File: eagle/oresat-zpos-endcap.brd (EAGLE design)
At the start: 106 x 106 mm, 47 parts, among them J7 1.27MM-SWD-CONNECTOR, U1 TPS63070, U2 TCAN330, U6 STM32F042K6, X1 16MHZ-2.5x2mm

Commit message: Oh right, the bottom of the board.
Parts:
- flipped CF1 to the bottom
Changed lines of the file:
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@@
 <attribute name="VALUE" x="59.71" y="29.575" size="1.27" layer="27" rot="R180"/>
 </element>
-<element name="CF1" library="oresat-connectors" package="CON-1.27-F-HARTING-1522012X601XXX" value="ORESAT-SOLARPANEL-12PIN" x="11.5" y="84.5" smashed="yes" rot="R90">
-<attribute name="NAME" x="8.325" y="92.485" size="0.635" layer="25" ratio="20" rot="R90"/>
-<attribute name="VALUE" x="9.595" y="92.485" size="0.635" layer="27" ratio="20" rot="R90"/>
+<element name="CF1" library="oresat-connectors" package="CON-1.27-F-HARTING-1522012X601XXX" value="ORESAT-SOLARPANEL-12PIN" x="11.5" y="84.5" smashed="yes" rot="MR90">
+<attribute name="NAME" x="14.675" y="92.485" size="0.635" layer="26" ratio="20" rot="MR90"/>
+<attribute name="VALUE" x="13.405" y="92.485" size="0.635" layer="28" ratio="20" rot="MR90"/>
 </element>
 </elements>

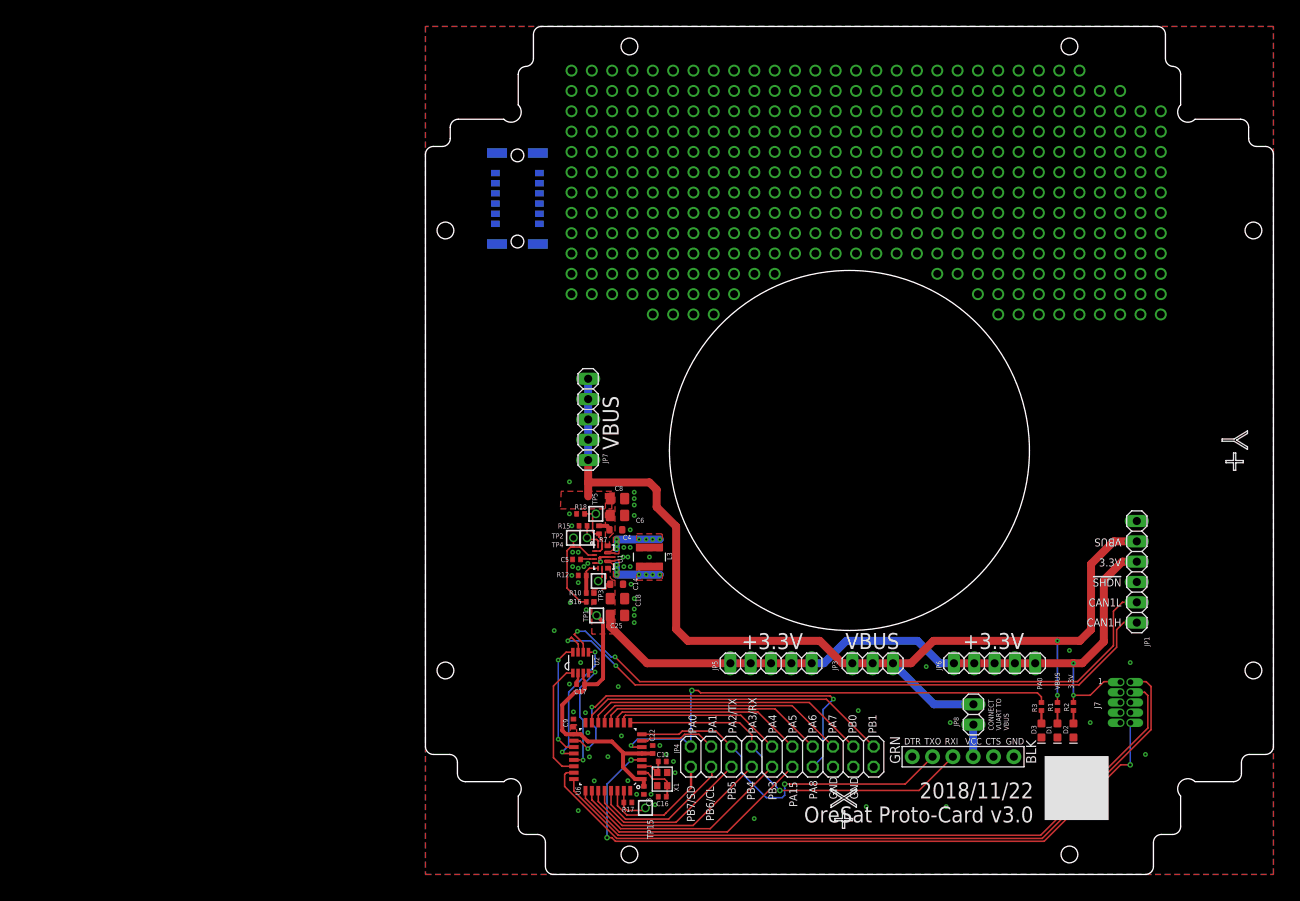
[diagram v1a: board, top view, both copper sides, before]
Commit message: Updated version info on the board and readme, and added picture.
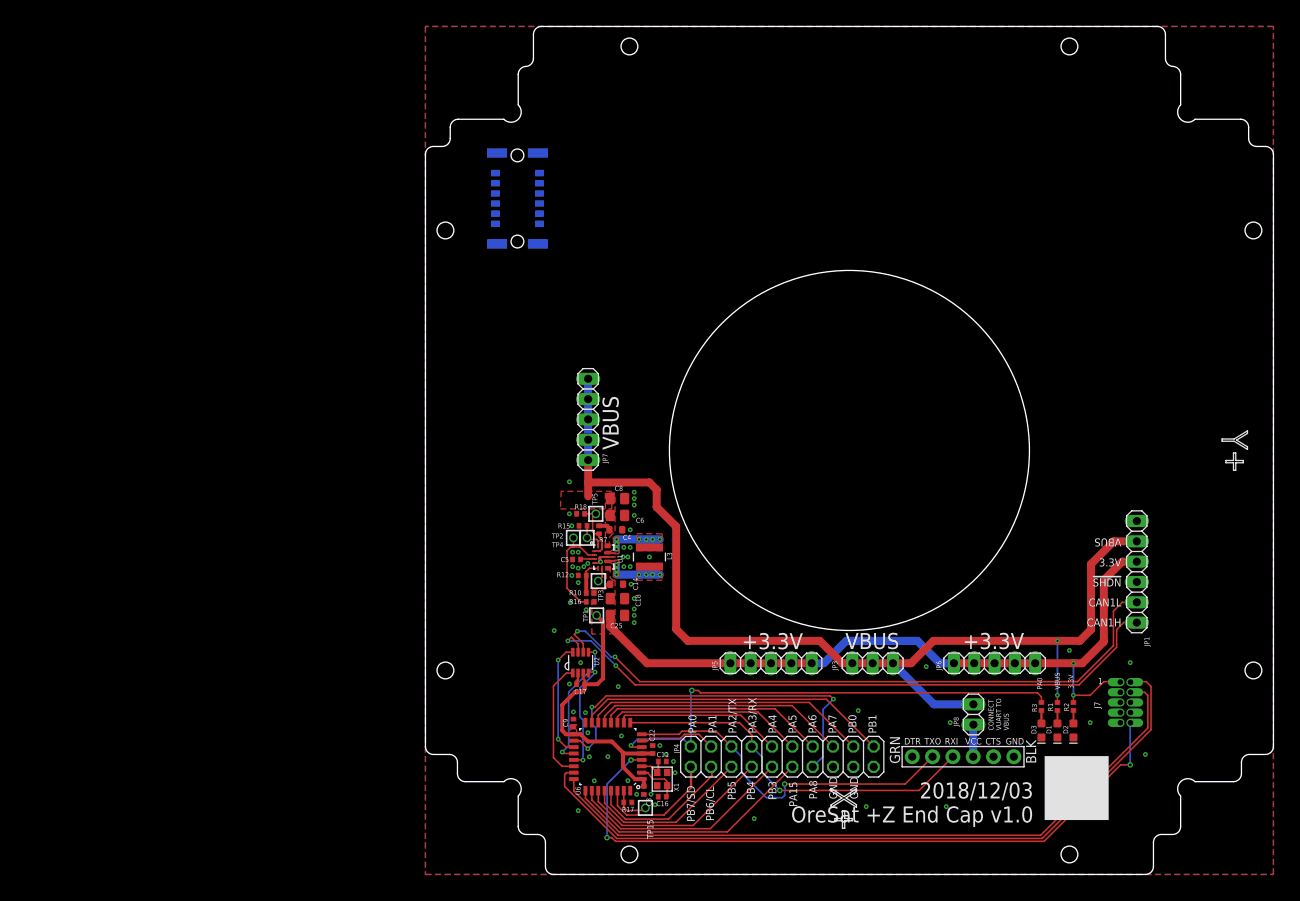
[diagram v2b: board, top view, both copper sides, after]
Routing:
- net GND: vias 114 -> 61
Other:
- board text added: "2018/12/03"
- board text added: "OreSat +Z End Cap v1.0"
- board text removed: "2018/11/22"
- board text removed: "OreSat Proto-Card v3.0"

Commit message: Not done, but checking in anyway. Lots left to do, trying to figure out where things go.
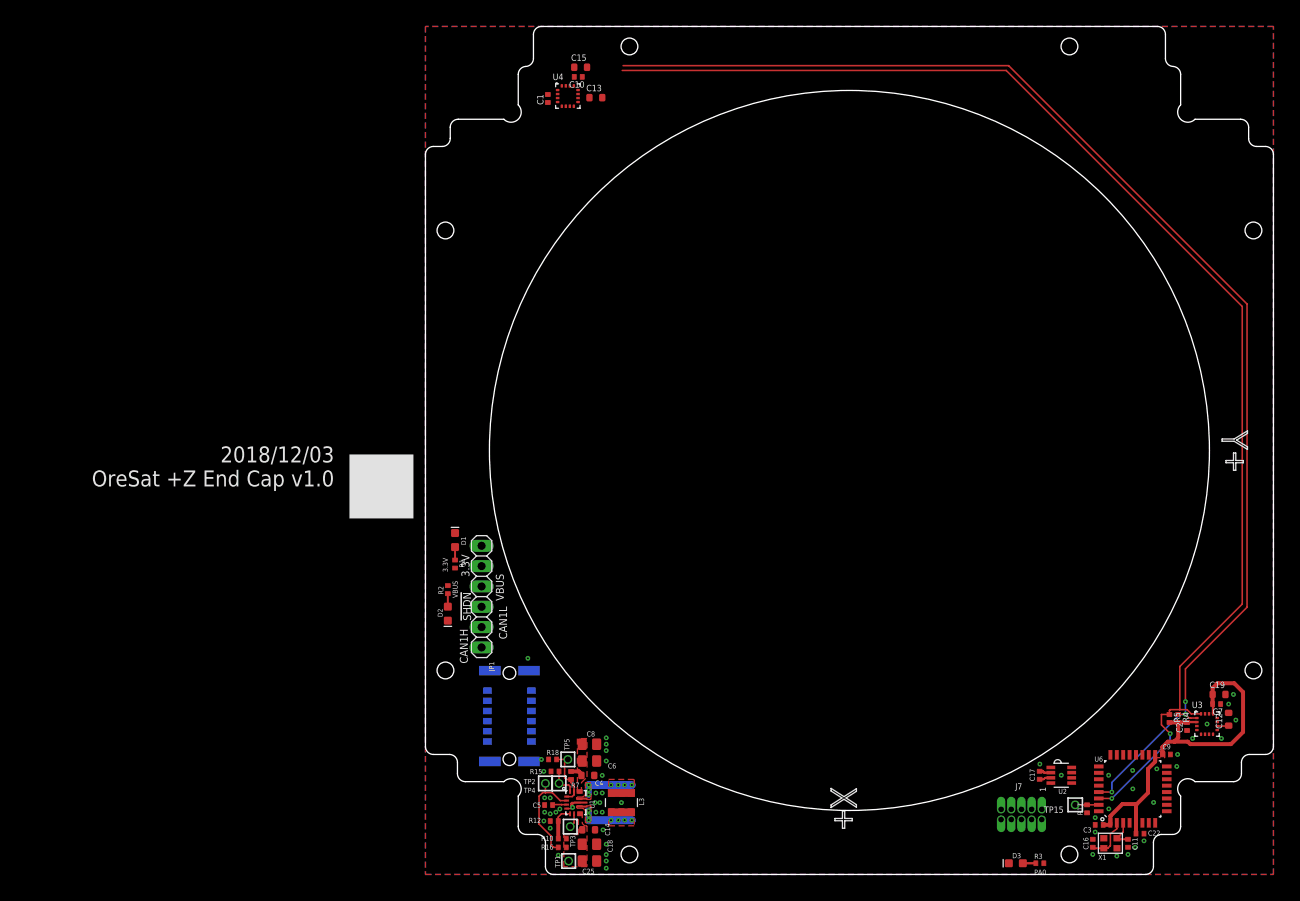
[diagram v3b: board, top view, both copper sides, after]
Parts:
- removed J5: (no value), SparkFun-Connectors:6_PIN_SERIAL_TARGET_SIDE_W_SILK
- removed JP3: (no value), pinhead:1X03
- removed JP4: (no value), pinhead:2X10
- removed JP5, JP6, JP7: (no value), pinhead:1X05
- removed JP8: (no value), pinhead:1X02
- added C1, C10, C2, C7: 100n, rcl_custom:.0402-B-NOSILK
- added C12, C13: 10u, oresat-rcl:.0603-B-NOSILK
- added C15, C19: 4.7u, oresat-rcl:.0603-B-NOSILK
- added R4, R5: 4.7k, rcl_custom:.0402-B-NOSILK
- added U3, U4: HMC5883L, monitor-v2:QLGA-16(3X3)
- CF1: value ORESAT-SOLARPANEL-12PIN -> J-HARWIN-M55-6021242R; device oresat-connectors:CON-1.27-F-HARTING-1522012X601XXX -> J-Harwin-M55-6021242R:HARWIN-M55-6021242R
- moved JP1 82.0 mm to (7.02, 34.7)
- moved D2 79.6 mm to (2.80, 32.6)
- moved R2 79.6 mm to (2.80, 35.6)
- moved D1 79.0 mm to (3.70, 41.8), turned to 90 degrees
- moved R1 77.4 mm to (3.70, 38.8), turned to 270 degrees
- moved C9 74.2 mm to (92.6, 15.0), turned to 180 degrees
- moved U6 65.7 mm to (88.4, 10.7), turned to 90 degrees
- moved CF1 64.7 mm to (10.5, 19.8)
- moved C22 61.8 mm to (89.3, 5.10), turned to 180 degrees
- moved U2 61.7 mm to (79.5, 12.4), turned to 270 degrees
- moved C11 59.1 mm to (87.8, 3.90), turned to 270 degrees
- moved C17 58.5 mm to (76.8, 12.4), turned to 270 degrees
- moved R17 57.4 mm to (82.7, 8.20), turned to 90 degrees
- moved C3 57.1 mm to (84.2, 6.20), turned to 0 degrees
- moved X1 56.6 mm to (85.6, 3.90), turned to 0 degrees
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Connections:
- removed net N$406: J5.P$4, JP8.2
- new net N$2: C12.1, U3.10
- new net N$3: U4.15
- new net N$4: U3.15
- new net N$5: C13.1, U4.10
- net 3.3V: now also C1.2, C10.2, C15.1, C19.1, C2.2, C7.2, R4.2, R5.2, U3.13, U3.2, U4.13, U4.2; no longer JP5.1, JP5.2, JP5.3, JP5.4, JP5.5, JP6.1, JP6.2, JP6.3, JP6.4, JP6.5
- net GND: now also C1.1, C10.1, C12.2, C13.2, C15.2, C19.2, C2.1, C7.1, CF1.P$1, CF1.P$2, CF1.P$3, CF1.P$4, U3.11, U3.9, U4.11, U4.9; no longer J5.P$6, JP4.15, JP4.17, JP4.19
- net PA0: no longer JP4.2
- net PA1: no longer JP4.4
- net PA15: no longer JP4.11
- net PA2/USART2_TX: no longer J5.P$2, JP4.6
- net PA3/USART2_RX: no longer J5.P$3, JP4.8
- net PA4: no longer JP4.10
- net PA5/SPI1_SCK: no longer JP4.12
- net PA6/SPI1_MISO: no longer JP4.14
- net PA7/SPI1_MOSI: no longer JP4.16
- net PA8: no longer JP4.13
- net PB0: no longer JP4.18
- net PB1: no longer JP4.20
- net PB3: no longer JP4.9
- net PB4: no longer JP4.7
- net PB5: no longer JP4.5
- net PB6/SCL: now also R4.1, U3.1, U4.1; no longer JP4.3
- net PB7/SDA: now also R5.1, U3.16, U4.16; no longer JP4.1
- net VBUS: no longer JP3.1, JP3.2, JP3.3, JP7.1, JP7.2, JP7.3, JP7.4, JP7.5, JP8.1
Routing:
- net PB7/SDA: track 15.6 -> 164.8 mm, vias 0 -> 2
- net PB6/SCL: track 18.5 -> 163.0 mm, vias 0 -> 3
- net VBUS: track 134.1 -> 1.62 mm, vias 2 -> 0
- net SWDIO: track 92.6 -> 0.00 mm
- net SWCLK: track 87.5 -> 0.00 mm
- net NRESET: track 87.1 -> 0.00 mm, vias 3 -> 0
- net CAN1_L: track 82.4 -> 0.00 mm, vias 2 -> 0
- net 3.3V: track 130.8 -> 49.0 mm, vias 2 -> 0
- net CAN1_H: track 80.8 -> 0.04 mm, vias 2 -> 0
- net PA0: track 61.4 -> 0.00 mm, vias 2 -> 0
- net PA8: track 48.5 -> 0.00 mm, vias 3 -> 0
- net PA3/USART2_RX: track 47.6 -> 0.00 mm, vias 1 -> 0
- net PA2/USART2_TX: track 44.1 -> 0.00 mm, vias 1 -> 0
- net PB1: track 39.4 -> 0.00 mm
- net PB0: track 35.8 -> 0.00 mm
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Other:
- outline, holes or cut-outs redrawn
- board text removed: "+3.3V"
- board text removed: "CONNECT VUART TO VBUS"
- board text removed: "GND"
- board text removed: "PA1"
- board text removed: "PA15"
- board text removed: "PA2/TX"
- board text removed: "PA3/RX"
- board text removed: "PA4"
- board text removed: "PA5"
- board text removed: "PA6"
- board text removed: "PA7"
- board text removed: "PA8"
- board text removed: "PB0"
- board text removed: "PB1"
- board text removed: "PB3"
- board text removed: "PB4"
- board text removed: "PB5"
- board text removed: "PB6/CL"
- board text removed: "PB7/SD"

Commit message: Removed SPS + uC blocks; only magnetometers remain on the end cap. Not great for future expandability, but moves uC to the end card where it's more useful.
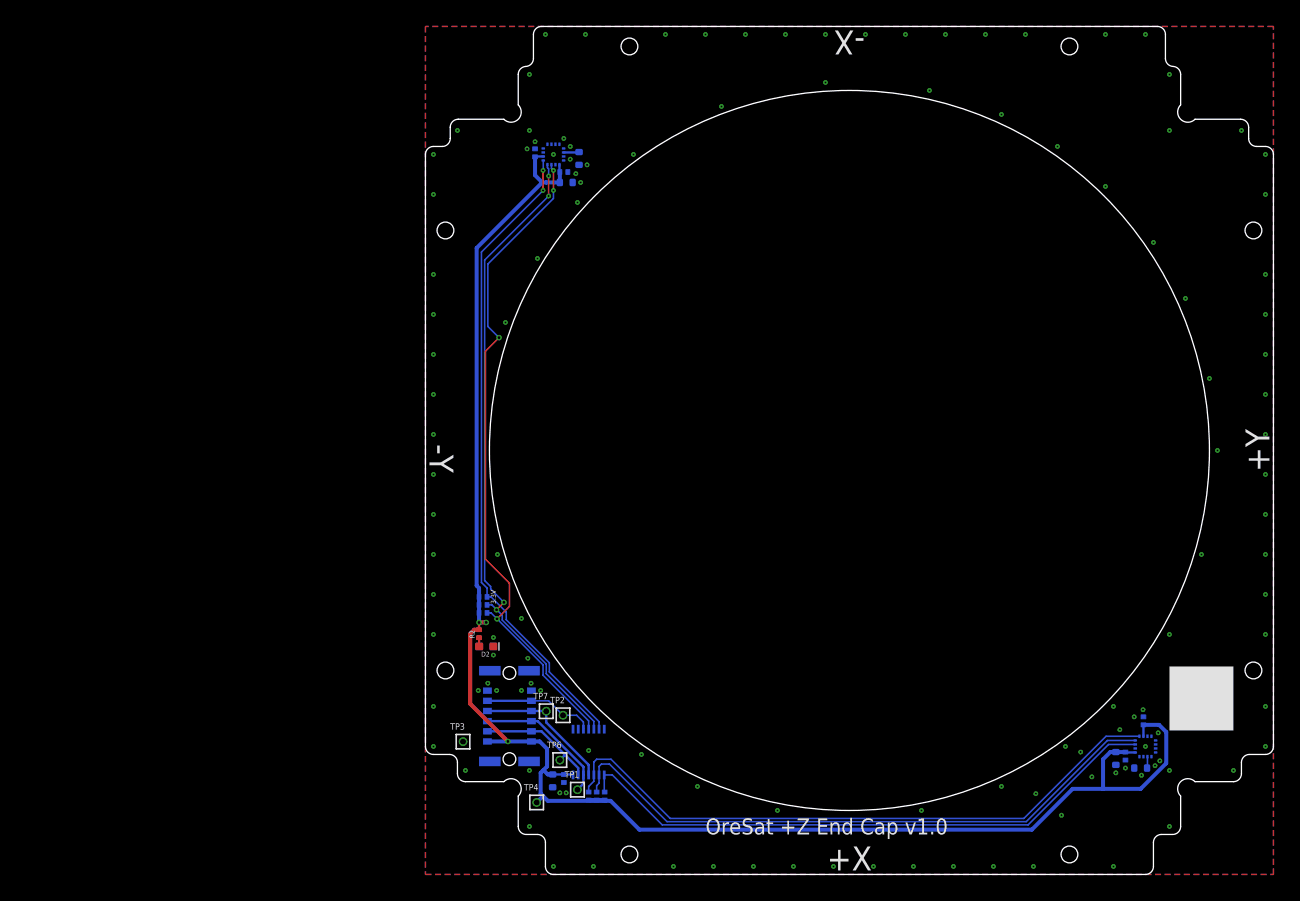
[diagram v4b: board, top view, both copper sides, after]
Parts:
- removed C11, C16: 20p, rcl_custom:.0402-B-NOSILK
- removed C14: 22u, oresat-rcl:.0603-B-NOSILK
- removed C17, C22, C5, C9: 100n, rcl_custom:.0402-B-NOSILK
- removed C18, C25: 22u, oresat-rcl:.0805-B-NOSILK
- removed C6, C8: 10u, oresat-rcl:.0805-B-NOSILK
- removed CF1: J-HARWIN-M55-6021242R, J-Harwin-M55-6021242R:HARWIN-M55-6021242R
- removed D1, D3: GREEN, SparkFun-LED:LED-0603
- removed J7: 1.27MM-SWD-CONNECTOR, J-CNC-3220-10-0100-00-ARM-SWD-port:1.27MM_2X5
- removed JP1: (no value), pinhead:1X06
- removed L3: 1.5 uH, L-Coilcraft-XFL4020:L-COILCRAFT-XFL4020
- removed R10: 470k, rcl_custom:.0402-B-NOSILK
- removed R12: 150k, rcl_custom:.0402-B-NOSILK
- removed R15, R17: 10k, rcl_custom:.0402-B-NOSILK
- removed R16, R18: NP, rcl_custom:.0402-B-NOSILK
- removed TP15, TP5: TEST-POINT, Tova:2MM-TEST-POINT
- removed U2: TCAN330, TCAN330:SOT23-8_TI-DCN
- removed U6: STM32F042K6, STM32F042K:QFP32-7X7
- removed X1: 16MHZ-2.5x2mm, low-gain-radio:CRYSTAL_2.5X2
- added CF2: J-HARWIN-M55-70X1242R, J-Harwin-M55-70X1242R-12pin-1.27mm-M-vertical:HARWIN-M55-70X1242R
- added R6: 4.7k, rcl_custom:.0402-B-NOSILK
- added TP6, TP7: TEST-POINT, Tova:2MM-TEST-POINT
- R1, R3: value 2.7k -> 4.7k
- R7: value 10k -> 4.7k
- U1: value TPS63070 -> TCA9543A-PW; device ic-pwr-tps63070x:TPS63070X -> U-TI-TCA9543A-I2C-2-to-1-multiplexer:TSSOP14-0.65-5.4X4.4MM
- moved R4 88.2 mm to (7.20, 34.7), flipped to the bottom, turned to 0 degrees
- moved R5 87.0 mm to (7.20, 33.7), flipped to the bottom, turned to 0 degrees
- moved C3 67.2 mm to (17.3, 12.0), flipped to the bottom, turned to 270 degrees
- moved R3 55.0 mm to (22.4, 9.80), flipped to the bottom, turned to 270 degrees
- moved TP3 17.1 mm to (4.70, 16.6)
- moved C19 15.2 mm to (86.3, 14.5), flipped to the bottom, turned to 270 degrees
- moved C15 14.5 mm to (17.6, 86.5), flipped to the bottom, turned to 180 degrees
- moved C7 13.1 mm to (87.5, 14.8), flipped to the bottom, turned to 270 degrees
- moved C12 12.6 mm to (89.4, 13.3), flipped to the bottom, turned to 0 degrees
- moved C10 12.0 mm to (17.3, 87.8), flipped to the bottom
- moved TP1 8.99 mm to (19.0, 10.6)
- moved TP2 8.80 mm to (17.2, 19.9)
- moved U3 8.19 mm to (90.0, 16.0), flipped to the bottom, turned to 270 degrees
- moved C13 7.88 mm to (19.2, 89.5), flipped to the bottom, turned to 270 degrees
- moved U4 7.52 mm to (16.0, 90.0), flipped to the bottom, turned to 180 degrees
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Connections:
- removed net BOOT: R17.2, TP15.1, U6.31
- removed net CAN1_H: JP1.1, U2.7
- removed net CAN1_L: JP1.2, U2.6
- removed net CAN_RX: U2.4, U6.21
- removed net CAN_SHDN: U2.5, U6.20
- removed net CAN_SILENT: U2.8, U6.19
- removed net CAN_TX: U2.1, U6.22
- removed net CRYSTALIN: C16.1, U6.2, X1.1
- removed net CRYSTALOUT: C11.1, U6.3, X1.3
- removed net N$1: D3.A, R3.1
- removed net N$270: D1.A, R1.1
- removed net N$3: U4.15
- removed net N$4: U3.15
- removed net NRESET: J7.!RESET, U6.4
- removed net PA0: R3.2, U6.6
- removed net PA1: U6.7
- removed net PA15: U6.25
- removed net PA2/USART2_TX: U6.8
- removed net PA3/USART2_RX: U6.9
- removed net PA4: U6.10
- removed net PA5/SPI1_SCK: U6.11
- removed net PA6/SPI1_MISO: U6.12
- removed net PA7/SPI1_MOSI: U6.13
- removed net PA8: U6.18
- removed net PB0: U6.14
- removed net PB1: U6.15
- removed net PB3: U6.26
- removed net PB4: U6.27
- removed net PB5: U6.28
- removed net PB6/SCL: R4.1, U3.1, U4.1, U6.29
- removed net PB7/SDA: R5.1, U3.16, U4.16, U6.30
- removed net SWCLK: J7.SWDCLK, U6.24
- removed net SWDIO: J7.SWDIO, U6.23
- removed net TPS-EN1: R18.2, R7.1, TP5.1, U1.1, U1.14
- removed net TPS-FB1: R10.1, R12.2, U1.5
- removed net TPS-FB3: TP3.1, U1.6
- removed net TPS-L3: L3.1, U1.11
- removed net TPS-L4: L3.2, U1.9
- removed net TPS-PG1: R16.1, TP2.1, U1.2
- removed net TPS-VAUX1: C5.1, U1.3
- removed net TPS-VSEL1: R15.2, TP4.1, U1.15
- removed net VBUS: C4.1, C6.1, C8.1, JP1.5, R1.2, R7.2, U1.12-13
- new net !I2C-RESET: CF2.3, CF2.4, TP2.1, U1.3
- new net !INT0: R1.1, U1.4, U4.15
- new net !INT1: R3.1, U1.8, U3.15
- new net I2C-!INT: CF2.5, CF2.6, TP7.1, U1.11
- new net I2C-SCL: CF2.7, CF2.8, TP1.1, U1.12
- new net I2C-SDA: CF2.10, CF2.9, TP6.1, U1.13
- new net SC1: R7.1, U1.10, U3.1
- new net SCL0: R4.1, U1.6, U4.1
- new net SD1: R6.1, U1.9, U3.16
- new net SDA0: R5.1, U1.5, U4.16
- net 3.3V: now also C1.1, C10.1, C2.1, C3.1, C4.1, C7.1, CF2.11, CF2.12, R1.2, R3.2, R6.2, R7.2, TP4.1, U1.14; no longer C1.2, C10.2, C14.1, C17.2, C18.1, C2.2, C22.2, C25.1, C3.2, C7.2, C9.2, J7.VTREF, JP1.4, R10.2, R16.2, TP1.1, U1.7-8, U2.3, U6.1, U6.17, U6.5
- net GND: now also C1.2, C10.2, C2.2, C3.2, C7.2, CF2.1, CF2.2, CF2.P$1, CF2.P$2, CF2.P$3, CF2.P$4, TP3.1, U1.1, U1.2, U1.7; no longer C1.1, C10.1, C11.2, C14.2, C16.2, C17.1, C18.2, C2.1, C22.1, C25.2, C3.1, C5.2, C6.2, C7.1, C8.2, C9.1, CF1.P$1, CF1.P$2, CF1.P$3, CF1.P$4, D1.C, D3.C, J7.GND, J7.GND@2, J7.GNDDET, JP1.6, R12.1, R15.1, R17.1, R18.1, U1.10, U1.4, U2.2, U6.16, U6.32, X1.2, X1.4
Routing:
- net PB7/SDA: track 164.8 -> 0.00 mm, vias 2 -> 0
- net PB6/SCL: track 163.0 -> 0.00 mm, vias 3 -> 0
- net 3.3V: track 49.0 -> 208.2 mm, vias 0 -> 3
- net !INT0: track 0.00 -> 83.5 mm, vias 0 -> 4
- net SDA0: track 0.00 -> 81.8 mm, vias 0 -> 4
- net SCL0: track 0.00 -> 80.7 mm, vias 0 -> 2
- net SC1: track 0.00 -> 79.7 mm
- net SD1: track 0.00 -> 77.7 mm
- net !INT1: track 0.00 -> 75.3 mm
- net I2C-SCL: track 0.00 -> 17.5 mm
- net I2C-!INT: track 0.00 -> 17.5 mm
- net I2C-SDA: track 0.00 -> 15.0 mm
- net !I2C-RESET: track 0.00 -> 14.1 mm
- net TPS-PG1: track 12.9 -> 0.00 mm
- net TPS-EN1: track 7.85 -> 0.00 mm
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- removed copper zone on layer 1, net 3.3V
- removed copper zone on layer 1, net TPS-L3
- removed copper zone on layer 1, net TPS-L4
- removed copper zone on layer 1, net VBUS
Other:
- board text added: "+X"
- board text added: "+Y"
- board text added: "-X"
- board text added: "-Y"
- board text removed: "!SHDN"
- board text removed: "2018/12/03"
- board text removed: "CAN1H"
- board text removed: "CAN1L"
- board text removed: "PA0"
- board text removed: "VBUS"
